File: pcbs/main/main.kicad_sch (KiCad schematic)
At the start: 0 parts

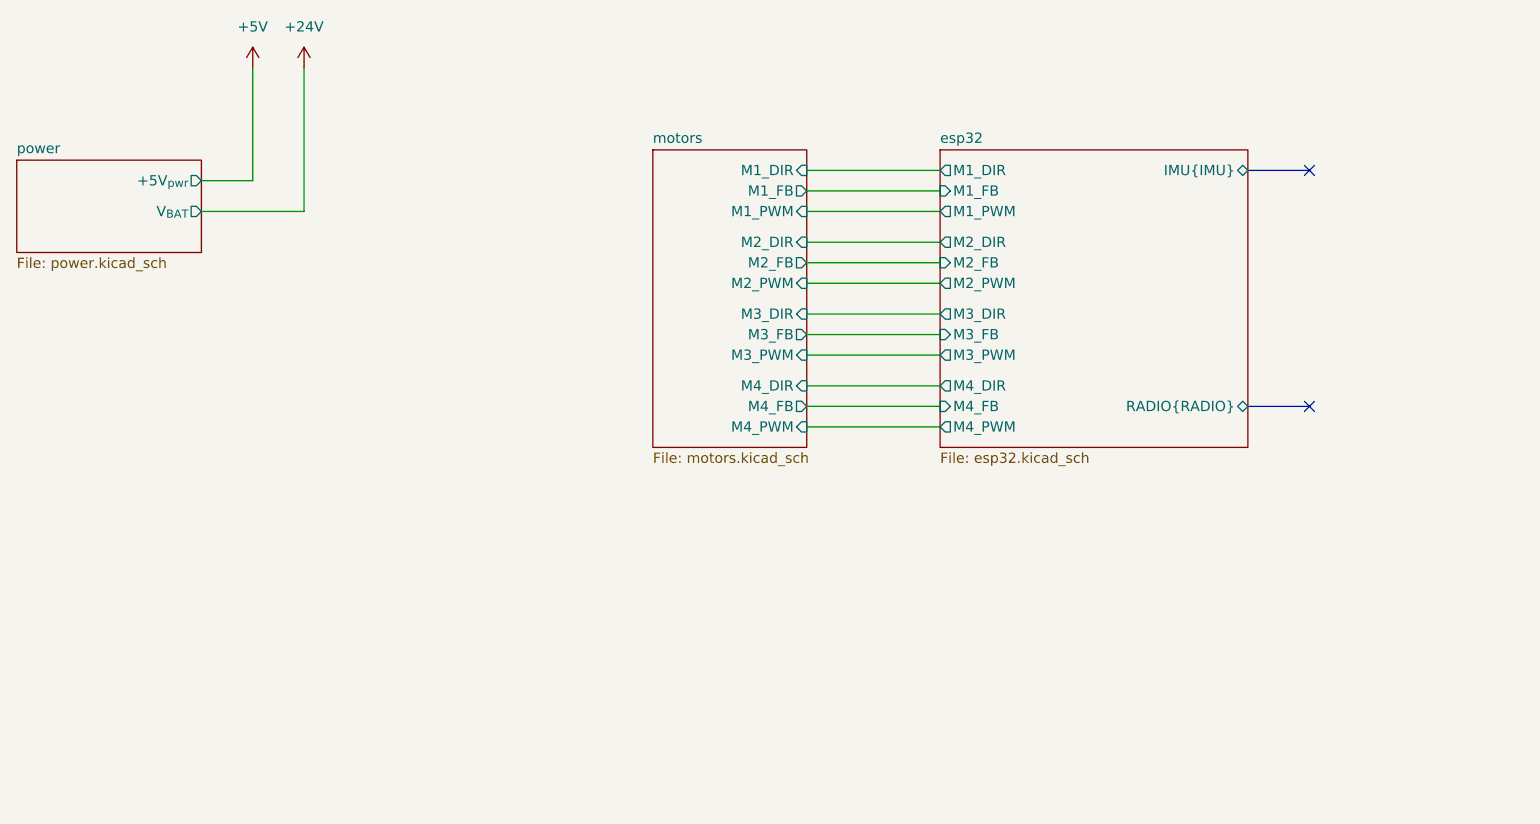
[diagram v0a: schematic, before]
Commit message: feat: radio and motor encoders
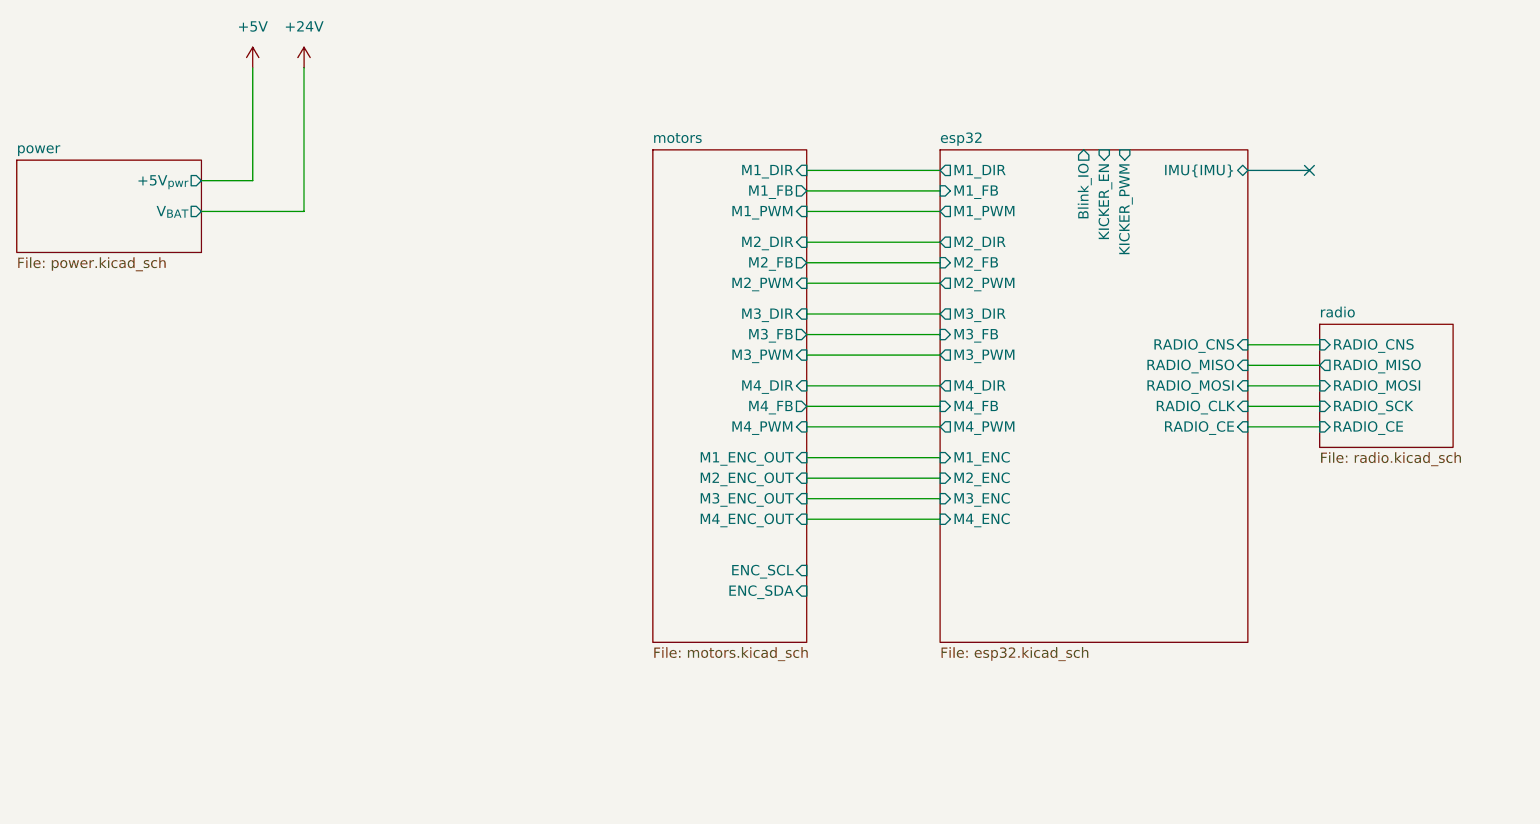
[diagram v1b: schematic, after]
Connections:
- no-connect marks 2 -> 1
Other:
- added sheet radio (radio.kicad_sch)
- sheet esp32 ports: added Blink_IO, KICKER_EN, KICKER_PWM, M1_ENC, M2_ENC, M3_ENC, M4_ENC, RADIO_CE, RADIO_CLK, RADIO_CNS, RADIO_MISO, RADIO_MOSI; removed RADIO{RADIO}
- sheet motors ports: added ENC_SCL, ENC_SDA, M1_ENC_OUT, M2_ENC_OUT, M3_ENC_OUT, M4_ENC_OUT; removed none

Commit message: feat: imu
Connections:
- no-connect marks 1 -> 0
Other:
- added sheet imu (imu.kicad_sch)
- sheet esp32 ports: added none; removed IMU{IMU}
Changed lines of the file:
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@@
 		(comment 3 "Author: Oxebots Team")
 	)
-	(no_connect
-		(at 182.88 50.8)
-	)
 	(wire
 		(pts
@@
 		(pts
 			(xy 120.65 64.77) (xy 137.16 64.77)
-		)
-		(stroke
-			(width 0)
-			(type default)
-		)
-	)
-	(bus
-		(pts
-			(xy 175.26 50.8) (xy 182.88 50.8)
 		)
 		(stroke
@@
 	)
 	(sheet
+		(at 184.15 49.53)
+		(size 16.51 12.7)
+		(exclude_from_sim no)
+		(in_bom yes)
+		(on_board yes)
+		(dnp no)
+		(fields_autoplaced yes)
+		(stroke
+			(width 0.1524)
+			(type solid)
+		)
+		(fill
+			(color 0 0 0 0.0000)
+		)
+		(property "Sheetname" "imu"
+			(at 184.15 48.8184 0)
+			(effects
+				(font
+					(size 1.27 1.27)
+				)
+				(justify left bottom)
+			)
+		)
+		(property "Sheetfile" "imu.kicad_sch"
+			(at 184.15 62.8146 0)
+			(effects
+				(font
+					(size 1.27 1.27)
+				)
+				(justify left top)
+			)
+		)
+		(instances
+			(project "main"
+				(path "/8ab8953a-1156-4e8b-85bc-154005b38a27"
+					(page "6")
+				)
+			)
+		)
+	)
+	(sheet
 		(at 137.16 48.26)
 		(size 38.1 60.96)
@@
 			)
 		)
-		(pin "IMU{IMU}" bidirectional
-			(at 175.26 50.8 0)
-			(effects
-				(font
-					(size 1.27 1.27)
-				)
-				(justify right)
-			)
-		)

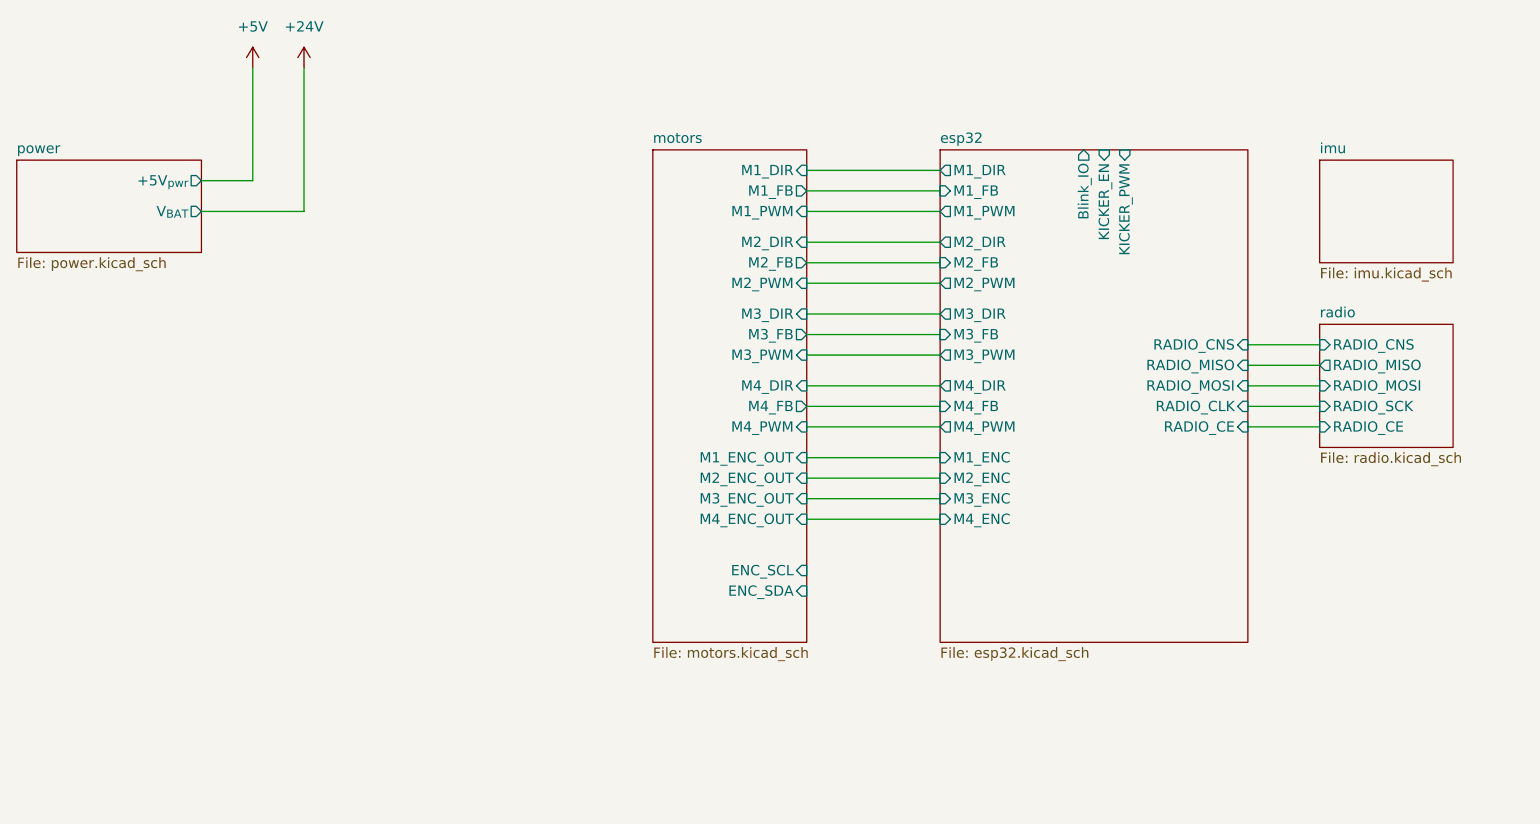
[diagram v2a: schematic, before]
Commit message: fea: add jumpers to I2C encoders config
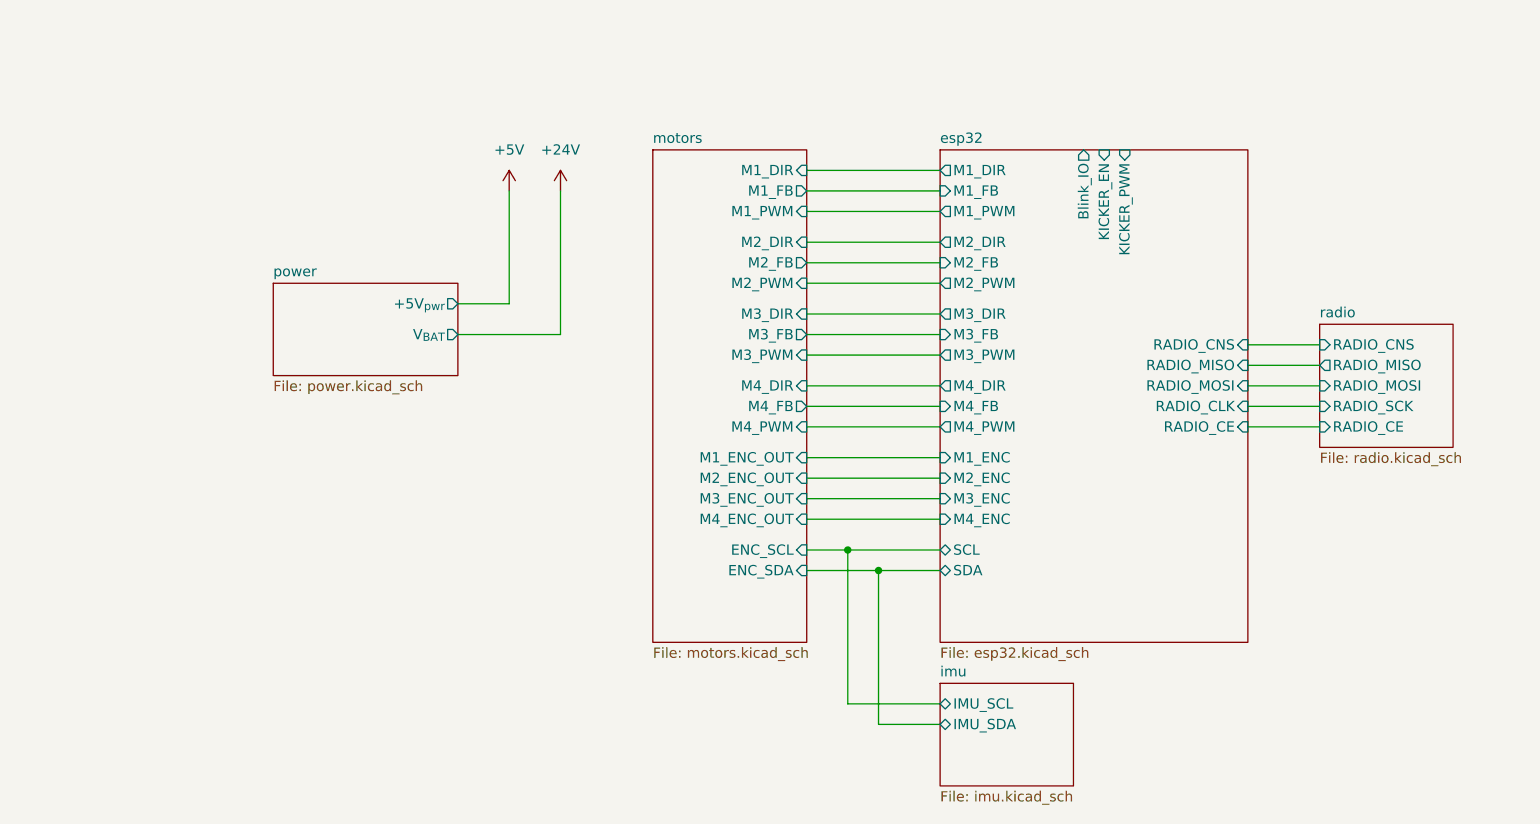
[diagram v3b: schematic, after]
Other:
- sheet esp32 ports: added SCL, SDA; removed none
- sheet imu ports: added IMU_SCL, IMU_SDA; removed none
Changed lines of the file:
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@@
 		(comment 3 "Author: Oxebots Team")
 	)
+	(junction
+		(at 129.54 100.33)
+		(diameter 0)
+		(color 0 0 0 0)
+	)
+	(junction
+		(at 125.73 97.79)
+		(diameter 0)
+		(color 0 0 0 0)
+	)
 	(wire
 		(pts
@@
 	(wire
 		(pts
+			(xy 129.54 119.38) (xy 137.16 119.38)
+		)
+		(stroke
+			(width 0)
+			(type default)
+		)
+	)
+	(wire
+		(pts
+			(xy 120.65 97.79) (xy 125.73 97.79)
+		)
+		(stroke
+			(width 0)
+			(type default)
+		)
+	)
+	(wire
+		(pts
 			(xy 120.65 68.58) (xy 137.16 68.58)
 		)
@@
 	(wire
 		(pts
-			(xy 58.42 55.88) (xy 58.42 38.1)
+			(xy 90.17 71.12) (xy 90.17 53.34)
 		)
 		(stroke
@@
 	(wire
 		(pts
-			(xy 45.72 55.88) (xy 58.42 55.88)
+			(xy 77.47 71.12) (xy 90.17 71.12)
 		)
 		(stroke
@@
 	(wire
 		(pts
+			(xy 125.73 97.79) (xy 137.16 97.79)
+		)
+		(stroke
+			(width 0)
+			(type default)
+		)
+	)
+	(wire
+		(pts
 			(xy 120.65 50.8) (xy 137.16 50.8)
 		)
@@
 	(wire
 		(pts
-			(xy 52.07 52.07) (xy 45.72 52.07)
+			(xy 83.82 67.31) (xy 77.47 67.31)
 		)
 		(stroke
@@
 	(wire
 		(pts
+			(xy 125.73 116.84) (xy 137.16 116.84)
+		)
+		(stroke
+			(width 0)
+			(type default)
+		)
+	)
+	(wire
+		(pts
 			(xy 120.65 77.47) (xy 137.16 77.47)
 		)
@@
 	(wire
 		(pts
+			(xy 125.73 97.79) (xy 125.73 116.84)
+		)
+		(stroke
+			(width 0)
+			(type default)
+		)
+	)
+	(wire
+		(pts
 			(xy 120.65 82.55) (xy 137.16 82.55)
 		)
@@
 	(wire
 		(pts
+			(xy 129.54 100.33) (xy 137.16 100.33)
+		)
+		(stroke
+			(width 0)
+			(type default)
+		)
+	)
+	(wire
+		(pts
 			(xy 120.65 71.12) (xy 137.16 71.12)
 		)
@@
 	(wire
 		(pts
-			(xy 52.07 38.1) (xy 52.07 52.07)
+			(xy 83.82 53.34) (xy 83.82 67.31)
 		)
 		(stroke
@@
 		(pts
 			(xy 175.26 72.39) (xy 184.15 72.39)
+		)
+		(stroke
+			(width 0)
+			(type default)
+		)
+	)
+	(wire
+		(pts
+			(xy 129.54 100.33) (xy 129.54 119.38)
+		)
+		(stroke
+			(width 0)
+			(type default)
+		)
+	)
+	(wire
+		(pts
+			(xy 120.65 100.33) (xy 129.54 100.33)
 		)
 		(stroke
@@
 	(symbol
 		(lib_id "power:+24V")
-		(at 58.42 38.1 0)
+		(at 90.17 53.34 0)
 		(unit 1)
 		(exclude_from_sim no)
@@
 		(fields_autoplaced yes)
 		(property "Reference" "#PWR02"
-			(at 58.42 41.91 0)
+			(at 90.17 57.15 0)
 			(effects
 				(font
@@
 		)
 		(property "Value" "+24V"
-			(at 58.42 33.02 0)
+			(at 90.17 48.26 0)
 			(effects
 				(font
@@
 		)
 		(property "Footprint" ""
-			(at 58.42 38.1 0)
+			(at 90.17 53.34 0)
 			(effects
 				(font
@@
 		)
 		(property "Datasheet" ""
-			(at 58.42 38.1 0)
+			(at 90.17 53.34 0)
 			(effects
 				(font
@@
 		)
 		(property "Description" "Power symbol creates a global label with name \"+24V\""
-			(at 58.42 38.1 0)
+			(at 90.17 53.34 0)
 			(effects
 				(font
@@
 	(symbol
 		(lib_id "power:+5V")
-		(at 52.07 38.1 0)
+		(at 83.82 53.34 0)
 		(unit 1)
 		(exclude_from_sim no)
@@
 		(fields_autoplaced yes)
 		(property "Reference" "#PWR01"
-			(at 52.07 41.91 0)
+			(at 83.82 57.15 0)
 			(effects
 				(font
@@
 		)
 		(property "Value" "+5V"
-			(at 52.07 33.02 0)
+			(at 83.82 48.26 0)
 			(effects
 				(font
@@
 		)
 		(property "Footprint" ""
-			(at 52.07 38.1 0)
+			(at 83.82 53.34 0)
 			(effects
 				(font
@@
 		)
 		(property "Datasheet" ""
-			(at 52.07 38.1 0)
+			(at 83.82 53.34 0)
 			(effects
 				(font
@@
 		)
 		(property "Description" "Power symbol creates a global label with name \"+5V\""
-			(at 52.07 38.1 0)
+			(at 83.82 53.34 0)
 			(effects
 				(font
@@
 		)
 		(pin "ENC_SCL" input
+			(at 120.65 97.79 0)
+			(effects
+				(font
+					(size 1.27 1.27)
+				)
+				(justify right)
+			)
+		)
+		(pin "ENC_SDA" input
 			(at 120.65 100.33 0)
-			(effects
-				(font
-					(size 1.27 1.27)
-				)
-				(justify right)
-			)
-		)
-		(pin "ENC_SDA" input
-			(at 120.65 102.87 0)
 			(effects
 				(font
@@
 	)
 	(sheet
-		(at 22.86 49.53)
+		(at 54.61 64.77)
 		(size 22.86 11.43)
 		(exclude_from_sim no)
@@
 		)
 		(property "Sheetname" "power"
-			(at 22.86 48.8184 0)
+			(at 54.61 64.0584 0)
 			(effects
 				(font
@@
 		)
 		(property "Sheetfile" "power.kicad_sch"
-			(at 22.86 61.5446 0)
+			(at 54.61 76.7846 0)
 			(effects
 				(font
@@
 		)
 		(pin "+5V_{pwr}" output
-			(at 45.72 52.07 0)
+			(at 77.47 67.31 0)
 			(effects
 				(font
@@
 		)
 		(pin "V_{BAT}" output
-			(at 45.72 55.88 0)
+			(at 77.47 71.12 0)
 			(effects
 				(font
@@
 	)
 	(sheet
-		(at 184.15 49.53)
+		(at 137.16 114.3)
 		(size 16.51 12.7)
 		(exclude_from_sim no)
@@
 		)
 		(property "Sheetname" "imu"
-			(at 184.15 48.8184 0)
+			(at 137.16 113.5884 0)
 			(effects
 				(font
@@
 		)
 		(property "Sheetfile" "imu.kicad_sch"
-			(at 184.15 62.8146 0)
+			(at 137.16 127.5846 0)
 			(effects
 				(font
@@
 				)
 				(justify left top)
+			)
+		)
+		(pin "IMU_SCL" bidirectional
+			(at 137.16 116.84 180)
+			(effects
+				(font
+					(size 1.27 1.27)
+				)
+				(justify left)
+			)
+		)
+		(pin "IMU_SDA" bidirectional
+			(at 137.16 119.38 180)
+			(effects
+				(font
+					(size 1.27 1.27)
+				)
+				(justify left)
 			)
 		)
@@
 			)
 		)
+		(pin "SCL" bidirectional
+			(at 137.16 97.79 180)
+			(effects
+				(font
+					(size 1.27 1.27)
+				)
+				(justify left)
+			)
+		)
+		(pin "SDA" bidirectional
+			(at 137.16 100.33 180)
+			(effects
+				(font
+					(size 1.27 1.27)
+				)
+				(justify left)
+			)
+		)
